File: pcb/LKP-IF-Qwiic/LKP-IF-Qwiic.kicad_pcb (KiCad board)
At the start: 2 copper layers, 41 x 36 mm, 9 parts, among them J1 JST SH, J2 JST SH, J3 LKP SWD .1" Extra Long, J4 LKP I/O .1" Extra Long, U1 TCA9406DCTR

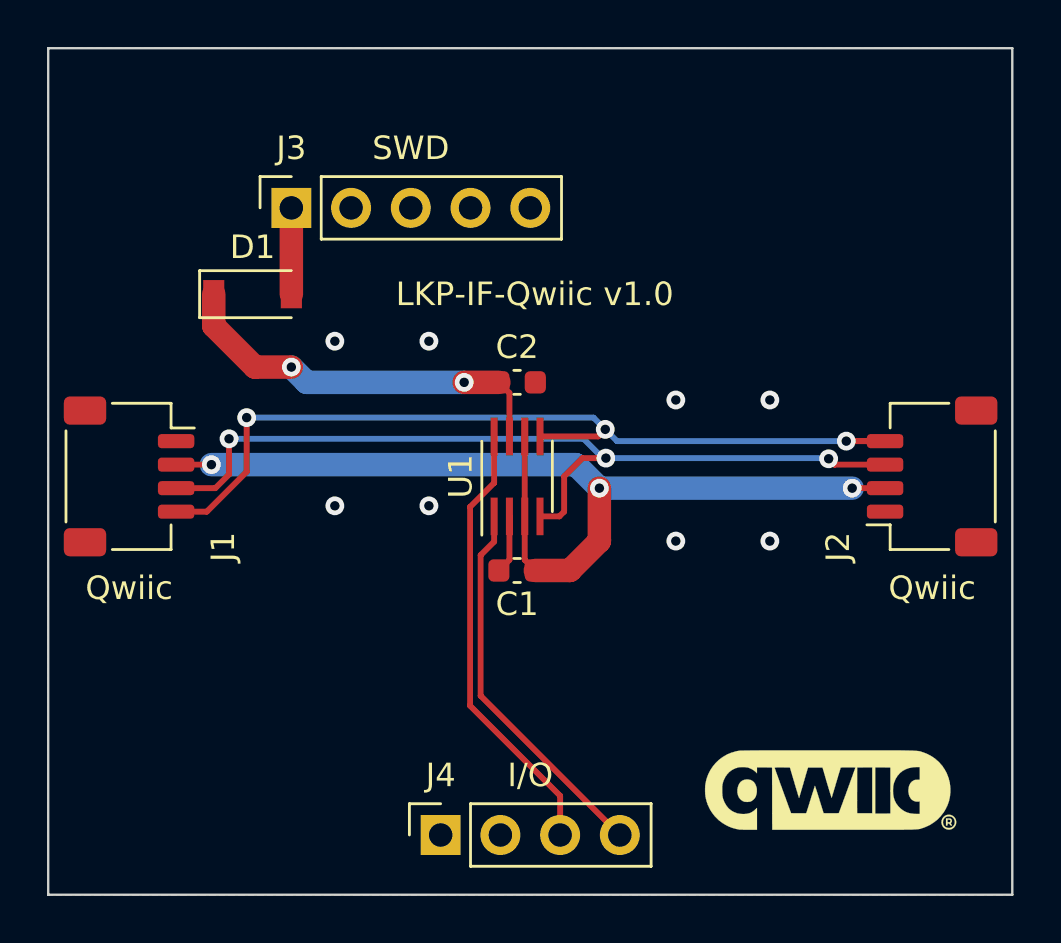
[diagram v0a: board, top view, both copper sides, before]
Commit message: LKP-IF-Qwiic: Add INT passthrough connector as an alternative to stacking headers.
README: Add notes about how to find the hard-to-find 18-pin male header.
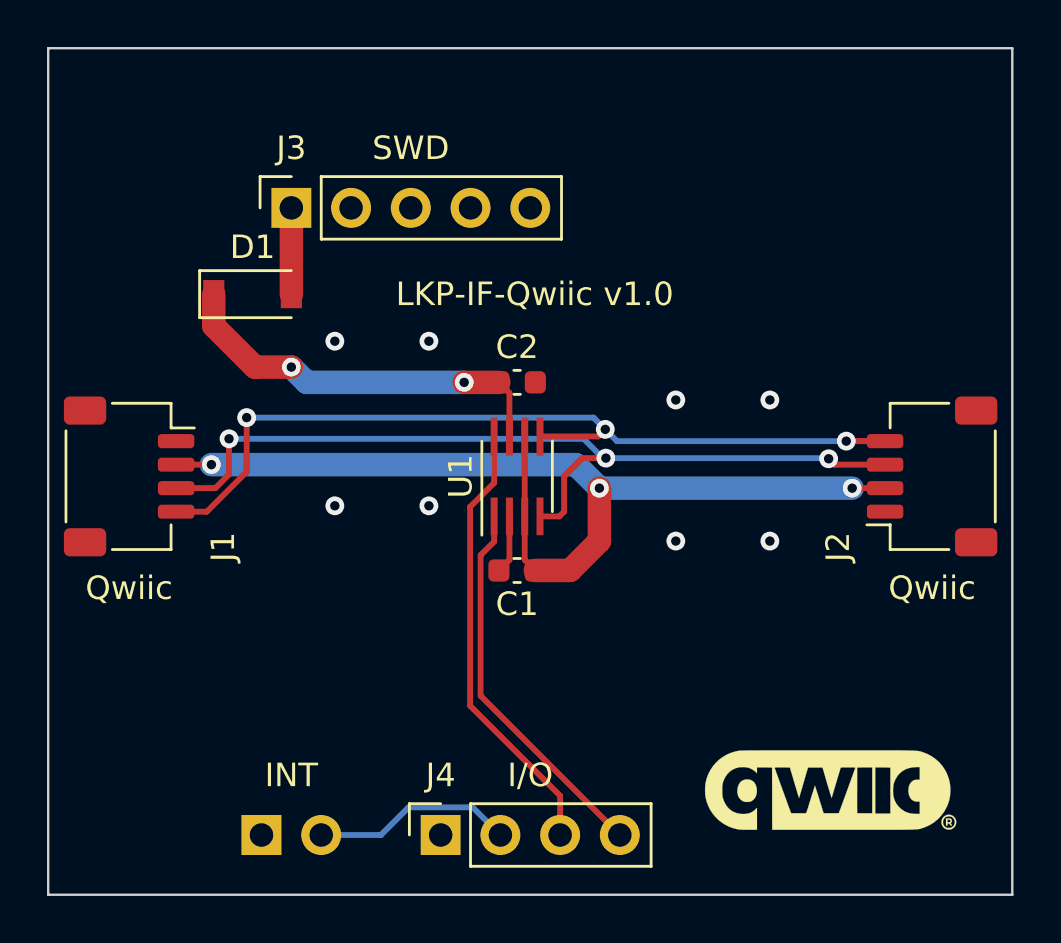
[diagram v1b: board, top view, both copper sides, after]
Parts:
- added J5: INT Passthrough, Connector_PinHeader_2.54mm:PinHeader_1x02_P2.54mm_Vertical, B.Cu at (139.1, 113.5)
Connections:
- J4 pad 2: Net-(J4-Pad2) -> /INT
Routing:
- net /INT: track 0.00 -> 8.59 mm
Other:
- board text added: "INT"
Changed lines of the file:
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@@
   (general
     (thickness 1.6)
-    (drawings 9)
-    (tracks 77)
+    (drawings 10)
+    (tracks 81)
     (zones 0)
-    (modules 9)
+    (modules 10)
     (nets 13)
   )
@@
     (visible_elements FFFFFF7F)
     (pcbplotparams
-      (layerselection 0x010fc_ffffffff)
+      (layerselection 0x010f0_ffffffff)
       (usegerberextensions false)
       (usegerberattributes true)
@@
       (outputformat 1)
       (mirror false)
-      (drillshape 1)
+      (drillshape 0)
       (scaleselection 1)
-      (outputdirectory ""))
+      (outputdirectory "out/"))
   )
   (net 0 "")
@@
   (net 9 /SDA_B)
   (net 10 /SCL_B)
-  (net 11 "Net-(J4-Pad2)")
-  (net 12 "Net-(D1-Pad2)")
+  (net 11 "Net-(D1-Pad2)")
+  (net 12 /INT)
   (net_class Default "This is the default net class."
     (clearance 0.2)
@@
     (uvia_dia 0.3)
     (uvia_drill 0.1)
+    (add_net /INT)
     (add_net /SCL_A)
     (add_net /SCL_B)
@@
     (add_net "Net-(J3-Pad4)")
     (add_net "Net-(J3-Pad5)")
-    (add_net "Net-(J4-Pad2)")
   )
   (net_class Power ""
@@
     (add_net GND)
     (add_net "Net-(D1-Pad2)")
+  )
+  (module Connector_PinHeader_2.54mm:PinHeader_1x02_P2.54mm_Vertical (layer B.Cu)
+    (at 139.07 113.46 270)
+    (descr "Through hole straight pin header, 1x02, 2.54mm pitch, single row")
+    (tags "Through hole pin header THT 1x02 2.54mm single row")
+    (fp_text reference J5 (at 0 2.33 90) (layer B.SilkS)
+      (effects (font (size 1 1) (thickness 0.15)) (justify mirror))
+    )
+    (fp_text value "INT Passthrough" (at 0 -4.87 90) (layer B.Fab)
+      (effects (font (size 1 1) (thickness 0.15)) (justify mirror))
+    )
+    (fp_text user %R (at 0 -1.27 180) (layer B.Fab)
+      (effects (font (size 1 1) (thickness 0.15)) (justify mirror))
+    )
+    (fp_line (start -0.635 1.27) (end 1.27 1.27) (layer B.Fab) (width 0.1))
+    (fp_line (start 1.27 1.27) (end 1.27 -3.81) (layer B.Fab) (width 0.1))
+    (fp_line (start 1.27 -3.81) (end -1.27 -3.81) (layer B.Fab) (width 0.1))
+    (fp_line (start -1.27 -3.81) (end -1.27 0.635) (layer B.Fab) (width 0.1))
+    (fp_line (start -1.27 0.635) (end -0.635 1.27) (layer B.Fab) (width 0.1))
+    (fp_line (start -1.33 -3.87) (end 1.33 -3.87) (layer B.SilkS) (width 0.12))
+    (fp_line (start -1.33 -1.27) (end -1.33 -3.87) (layer B.SilkS) (width 0.12))
+    (fp_line (start 1.33 -1.27) (end 1.33 -3.87) (layer B.SilkS) (width 0.12))
+    (fp_line (start -1.33 -1.27) (end 1.33 -1.27) (layer B.SilkS) (width 0.12))
+    (fp_line (start -1.33 0) (end -1.33 1.33) (layer B.SilkS) (width 0.12))
+    (fp_line (start -1.33 1.33) (end 0 1.33) (layer B.SilkS) (width 0.12))
+    (fp_line (start -1.8 1.8) (end -1.8 -4.35) (layer B.CrtYd) (width 0.05))
+    (fp_line (start -1.8 -4.35) (end 1.8 -4.35) (layer B.CrtYd) (width 0.05))
+    (fp_line (start 1.8 -4.35) (end 1.8 1.8) (layer B.CrtYd) (width 0.05))
+    (fp_line (start 1.8 1.8) (end -1.8 1.8) (layer B.CrtYd) (width 0.05))
+    (pad 2 thru_hole oval (at 0 -2.54 270) (size 1.7 1.7) (drill 1) (layers *.Cu *.Mask)
+      (net 12 /INT))
+    (pad 1 thru_hole rect (at 0 0 270) (size 1.7 1.7) (drill 1) (layers *.Cu *.Mask)
+      (net 1 GND))
+    (model ${KISYS3DMOD}/Connector_PinHeader_2.54mm.3dshapes/PinHeader_1x02_P2.54mm_Vertical.wrl
+      (at (xyz 0 0 0))
+      (scale (xyz 1 1 1))
+      (rotate (xyz 0 0 0))
+    )
   )
   (module Diode_SMD:D_SOD-123 (layer F.Cu)
@@
     )
     (pad 2 smd rect (at 1.65 0) (size 0.9 1.2) (layers F.Cu F.Paste F.Mask)
-      (net 12 "Net-(D1-Pad2)"))
+      (net 11 "Net-(D1-Pad2)"))
     (pad 1 smd rect (at -1.65 0) (size 0.9 1.2) (layers F.Cu F.Paste F.Mask)
       (net 3 +5V))
@@
       (effects (font (size 1 1) (thickness 0.15)))
     )
-    (pad MP smd roundrect (at 2.8 1.875 90) (size 1.2 1.8) (layers F.Cu F.Paste F.Mask) (roundrect_rratio 0.208333))
-    (pad MP smd roundrect (at -2.8 1.875 90) (size 1.2 1.8) (layers F.Cu F.Paste F.Mask) (roundrect_rratio 0.208333))
+    (pad MP smd roundrect (at 2.8 1.875 90) (size 1.2 1.8) (layers F.Cu F.Paste F.Mask) (roundrect_rratio 0.2083325))
+    (pad MP smd roundrect (at -2.8 1.875 90) (size 1.2 1.8) (layers F.Cu F.Paste F.Mask) (roundrect_rratio 0.2083325))
     (pad 4 smd roundrect (at 1.5 -2 90) (size 0.6 1.55) (layers F.Cu F.Paste F.Mask) (roundrect_rratio 0.25)
       (net 4 /SCL_A))
@@
       (effects (font (size 1 1) (thickness 0.15)))
     )
-    (pad MP smd roundrect (at 2.8 1.875 270) (size 1.2 1.8) (layers F.Cu F.Paste F.Mask) (roundrect_rratio 0.208333))
-    (pad MP smd roundrect (at -2.8 1.875 270) (size 1.2 1.8) (layers F.Cu F.Paste F.Mask) (roundrect_rratio 0.208333))
+    (pad MP smd roundrect (at 2.8 1.875 270) (size 1.2 1.8) (layers F.Cu F.Paste F.Mask) (roundrect_rratio 0.2083325))
+    (pad MP smd roundrect (at -2.8 1.875 270) (size 1.2 1.8) (layers F.Cu F.Paste F.Mask) (roundrect_rratio 0.2083325))
     (pad 4 smd roundrect (at 1.5 -2 270) (size 0.6 1.55) (layers F.Cu F.Paste F.Mask) (roundrect_rratio 0.25)
       (net 4 /SCL_A))
@@
       (net 10 /SCL_B))
     (pad 2 thru_hole oval (at 0 2.54 90) (size 1.7 1.7) (drill 1) (layers *.Cu *.Mask)
-      (net 11 "Net-(J4-Pad2)"))
+      (net 12 /INT))
     (pad 1 thru_hole rect (at 0 0 90) (size 1.7 1.7) (drill 1) (layers *.Cu *.Mask)
       (net 1 GND))
@@
       (net 1 GND))
     (pad 1 thru_hole rect (at 0 0 90) (size 1.7 1.7) (drill 1) (layers *.Cu *.Mask)
-      (net 12 "Net-(D1-Pad2)"))
+      (net 11 "Net-(D1-Pad2)"))
     (model ${KISYS3DMOD}/Connector_PinSocket_2.54mm.3dshapes/PinSocket_1x05_P2.54mm_Vertical.wrl
       (at (xyz 0 0 0))
@@
       (rotate (xyz 0 0 0))
     )
+  )
+  (gr_text INT (at 140.34 110.92) (layer F.SilkS)
+    (effects (font (size 1 1) (thickness 0.15)))
   )
   (gr_text Qwiic (at 167.59 102.96) (layer F.SilkS)
@@
   (segment (start 148.965 98.485) (end 147.93998 99.51002) (width 0.25) (layer F.Cu) (net 10))
   (segment (start 148.965 96.51) (end 148.965 98.485) (width 0.25) (layer F.Cu) (net 10))
-  (segment (start 140.34 90.46) (end 140.34 86.79) (width 1) (layer F.Cu) (net 12))
+  (segment (start 140.34 90.46) (end 140.34 86.79) (width 1) (layer F.Cu) (net 11))
+  (segment (start 148.054999 112.284999) (end 145.325001 112.284999) (width 0.25) (layer B.Cu) (net 12))
+  (segment (start 149.23 113.46) (end 148.054999 112.284999) (width 0.25) (layer B.Cu) (net 12))
+  (segment (start 144.15 113.46) (end 141.61 113.46) (width 0.25) (layer B.Cu) (net 12))
+  (segment (start 145.325001 112.284999) (end 144.15 113.46) (width 0.25) (layer B.Cu) (net 12))
   (zone (net 1) (net_name GND) (layer F.Cu) (hatch edge 0.508)
     (connect_pads (clearance 0.508))

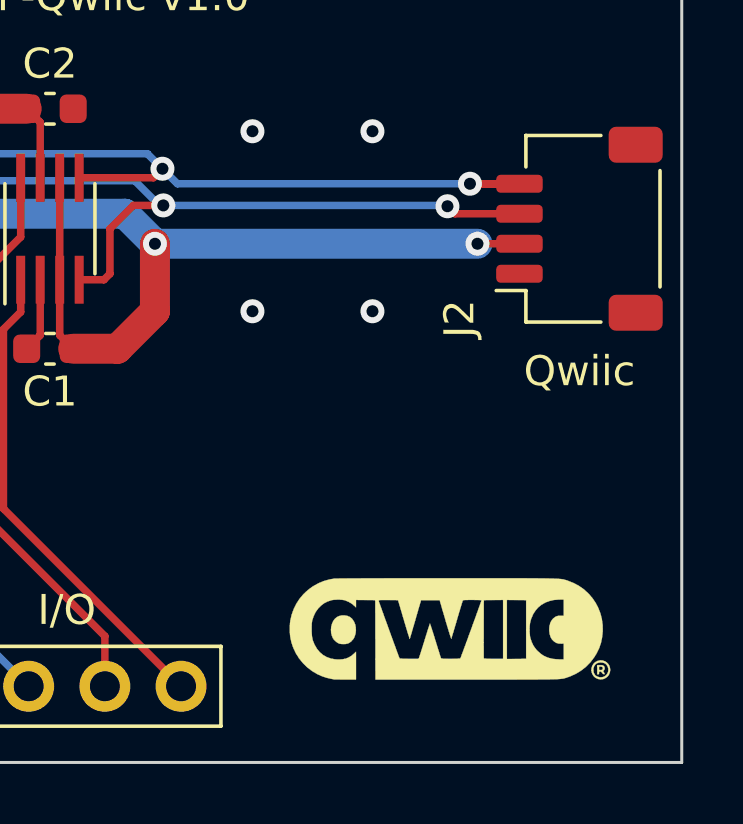
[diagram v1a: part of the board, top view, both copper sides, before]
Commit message: Update all active projects to KiCad 6.
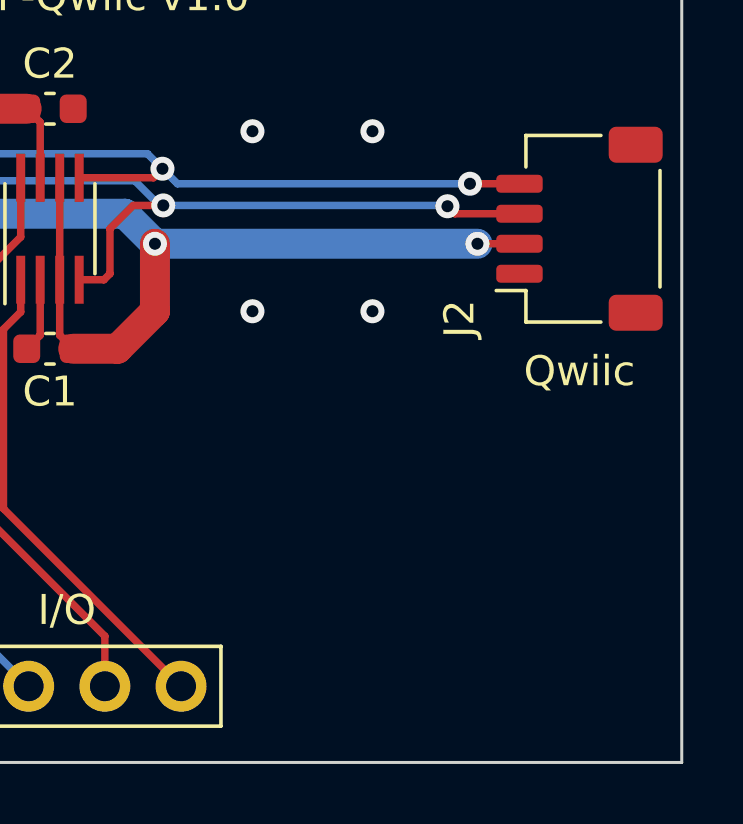
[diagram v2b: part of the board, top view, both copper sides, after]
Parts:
- removed G***: LOGO, private:Qwiic-Logo
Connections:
- J3 pad 3: Net-(J3-Pad3) -> unconnected-(J3-Pad3)
- J3 pad 4: Net-(J3-Pad4) -> unconnected-(J3-Pad4)
- J3 pad 5: Net-(J3-Pad5) -> unconnected-(J3-Pad5)
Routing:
- net /SCL_A: track 38.2 -> 36.6 mm
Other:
- net class Default removed
- net class Power removed
